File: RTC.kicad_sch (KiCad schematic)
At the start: 10 parts, among them J17 Molex 470531000, J2 Molex 470531000, J3 Molex 470531000, J6 Molex 470531000, U2 EMC2305-1-AP-TR

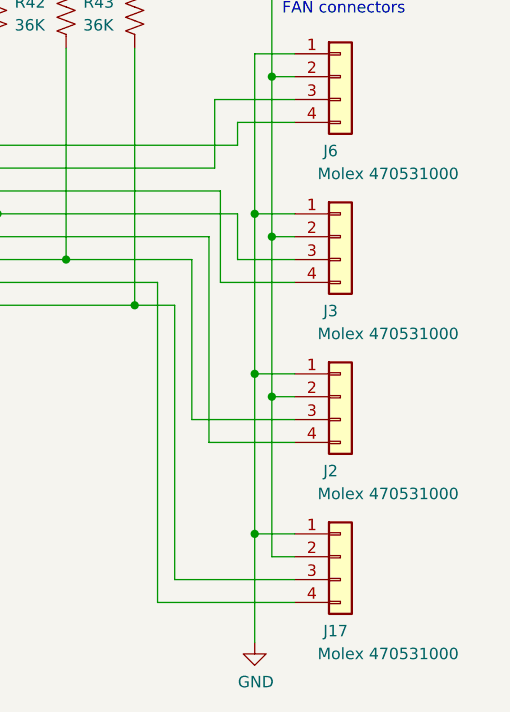
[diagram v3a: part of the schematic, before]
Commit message: added the right board outline. rotated the CM4. switched to single-shroud RA fan connectors
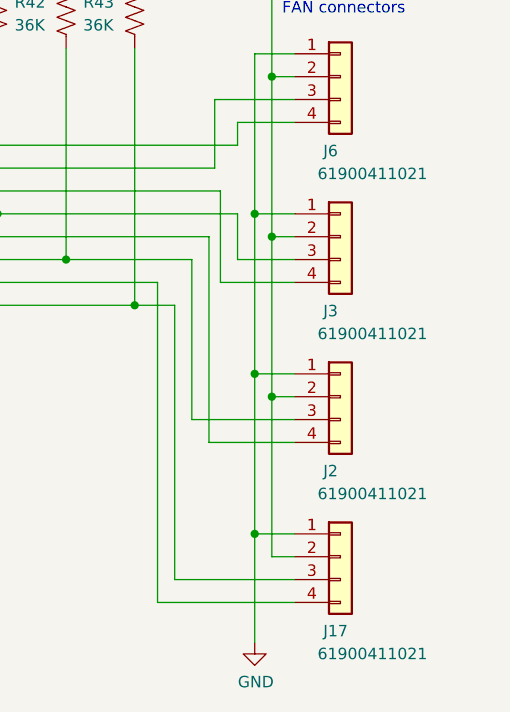
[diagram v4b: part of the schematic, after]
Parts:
- J17, J2, J3: value Molex 470531000 -> 61900411021; footprint Connector:FanPinHeader_1x04_P2.54mm_Vertical -> bitcart:CONN_61900411021_WRE; DK WM4330-ND -> 732-2701-ND; Field4 Farnell -> (none); Field5 2313705 -> (none); Field6 470531000 -> (none); Field7 Molex -> (none); PARTNO 470531000 -> 61900411021
- J6: value Molex 470531000 -> 61900411021; footprint Connector:FanPinHeader_1x04_P2.54mm_Vertical -> bitcart:CONN_61900411021_WRE; DK WM4330-ND -> 732-2701-ND; Field6 470531000 -> (none); PARTNO 470531000 -> 61900411021
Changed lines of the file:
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@@
       (effects (font (size 1.27 1.27)) (justify left))
     )
-    (property "Value" "Molex 470531000" (at 194.31 121.285 0)
-      (effects (font (size 1.27 1.27)) (justify left))
-    )
-    (property "Footprint" "Connector:FanPinHeader_1x04_P2.54mm_Vertical" (at 196.85 110.49 0)
+    (property "Value" "61900411021" (at 194.31 121.285 0)
+      (effects (font (size 1.27 1.27)) (justify left))
+    )
+    (property "Footprint" "bitcart:CONN_61900411021_WRE" (at 196.85 110.49 0)
       (effects (font (size 1.27 1.27)) hide)
     )
@@
       (effects (font (size 1.27 1.27)) hide)
     )
-    (property "Field4" "Farnell" (at 196.85 110.49 0)
-      (effects (font (size 1.27 1.27)) hide)
-    )
-    (property "Field5" "	2313705" (at 196.85 110.49 0)
-      (effects (font (size 1.27 1.27)) hide)
-    )
-    (property "Field6" "470531000" (at 196.85 110.49 0)
-      (effects (font (size 1.27 1.27)) hide)
-    )
-    (property "Field7" "Molex" (at 196.85 110.49 0)
-      (effects (font (size 1.27 1.27)) hide)
-    )
-    (property "Part Description" "" (at 196.85 110.49 0)
-      (effects (font (size 1.27 1.27)) hide)
-    )
-    (property "DK" "WM4330-ND" (at 196.85 110.49 0)
-      (effects (font (size 1.27 1.27)) hide)
-    )
-    (property "PARTNO" "470531000" (at 196.85 110.49 0)
+    (property "DK" "732-2701-ND" (at 196.85 110.49 0)
+      (effects (font (size 1.27 1.27)) hide)
+    )
+    (property "PARTNO" "61900411021" (at 196.85 110.49 0)
       (effects (font (size 1.27 1.27)) hide)
     )
@@
       (effects (font (size 1.27 1.27)) (justify left))
     )
-    (property "Value" "Molex 470531000" (at 194.31 67.945 0)
-      (effects (font (size 1.27 1.27)) (justify left))
-    )
-    (property "Footprint" "Connector:FanPinHeader_1x04_P2.54mm_Vertical" (at 196.85 57.15 0)
+    (property "Value" "61900411021" (at 194.31 67.945 0)
+      (effects (font (size 1.27 1.27)) (justify left))
+    )
+    (property "Footprint" "bitcart:CONN_61900411021_WRE" (at 196.85 57.15 0)
       (effects (font (size 1.27 1.27)) hide)
     )
@@
       (effects (font (size 1.27 1.27)) hide)
     )
-    (property "DK" "WM4330-ND" (at 196.85 57.15 0)
-      (effects (font (size 1.27 1.27)) hide)
-    )
-    (property "Field6" "470531000" (at 196.85 57.15 0)
-      (effects (font (size 1.27 1.27)) hide)
-    )
-    (property "PARTNO" "470531000" (at 196.85 57.15 0)
+    (property "DK" "732-2701-ND" (at 196.85 57.15 0)
+      (effects (font (size 1.27 1.27)) hide)
+    )
+    (property "PARTNO" "61900411021" (at 196.85 57.15 0)
       (effects (font (size 1.27 1.27)) hide)
     )
@@
       (effects (font (size 1.27 1.27)) (justify left))
     )
-    (property "Value" "Molex 470531000" (at 194.31 103.505 0)
-      (effects (font (size 1.27 1.27)) (justify left))
-    )
-    (property "Footprint" "Connector:FanPinHeader_1x04_P2.54mm_Vertical" (at 196.85 92.71 0)
+    (property "Value" "61900411021" (at 194.31 103.505 0)
+      (effects (font (size 1.27 1.27)) (justify left))
+    )
+    (property "Footprint" "bitcart:CONN_61900411021_WRE" (at 196.85 92.71 0)
       (effects (font (size 1.27 1.27)) hide)
     )
@@
       (effects (font (size 1.27 1.27)) hide)
     )
-    (property "Field4" "Farnell" (at 196.85 92.71 0)
-      (effects (font (size 1.27 1.27)) hide)
-    )
-    (property "Field5" "	2313705" (at 196.85 92.71 0)
-      (effects (font (size 1.27 1.27)) hide)
-    )
-    (property "Field6" "470531000" (at 196.85 92.71 0)
-      (effects (font (size 1.27 1.27)) hide)
-    )
-    (property "Field7" "Molex" (at 196.85 92.71 0)
-      (effects (font (size 1.27 1.27)) hide)
-    )
-    (property "Part Description" "" (at 196.85 92.71 0)
-      (effects (font (size 1.27 1.27)) hide)
-    )
-    (property "DK" "WM4330-ND" (at 196.85 92.71 0)
-      (effects (font (size 1.27 1.27)) hide)
-    )
-    (property "PARTNO" "470531000" (at 196.85 92.71 0)
+    (property "DK" "732-2701-ND" (at 196.85 92.71 0)
+      (effects (font (size 1.27 1.27)) hide)
+    )
+    (property "PARTNO" "61900411021" (at 196.85 92.71 0)
       (effects (font (size 1.27 1.27)) hide)
     )
@@
       (effects (font (size 1.27 1.27)) (justify left))
     )
-    (property "Value" "Molex 470531000" (at 194.31 85.725 0)
-      (effects (font (size 1.27 1.27)) (justify left))
-    )
-    (property "Footprint" "Connector:FanPinHeader_1x04_P2.54mm_Vertical" (at 196.85 74.93 0)
+    (property "Value" "61900411021" (at 194.31 85.725 0)
+      (effects (font (size 1.27 1.27)) (justify left))
+    )
+    (property "Footprint" "bitcart:CONN_61900411021_WRE" (at 196.85 74.93 0)
       (effects (font (size 1.27 1.27)) hide)
     )
@@
       (effects (font (size 1.27 1.27)) hide)
     )
-    (property "Field4" "Farnell" (at 196.85 74.93 0)
-      (effects (font (size 1.27 1.27)) hide)
-    )
-    (property "Field5" "	2313705" (at 196.85 74.93 0)
-      (effects (font (size 1.27 1.27)) hide)
-    )
-    (property "Field6" "470531000" (at 196.85 74.93 0)
-      (effects (font (size 1.27 1.27)) hide)
-    )
-    (property "Field7" "Molex" (at 196.85 74.93 0)
-      (effects (font (size 1.27 1.27)) hide)
-    )
-    (property "Part Description" "" (at 196.85 74.93 0)
-      (effects (font (size 1.27 1.27)) hide)
-    )
-    (property "DK" "WM4330-ND" (at 196.85 74.93 0)
-      (effects (font (size 1.27 1.27)) hide)
-    )
-    (property "PARTNO" "470531000" (at 196.85 74.93 0)
-      (effects (font (size 1.27 1.27)) hide)
-    )
+    (property "DK" "732-2701-ND" (at 196.85 74.93 0)
+      (effects (font (size 1.27 1.27)) hide)
+    )
+    (property "PARTNO" "61900411021" (at 196.85 74.93 0)
+      (effects (font (size 1.27 1.27)) hide)
+    )

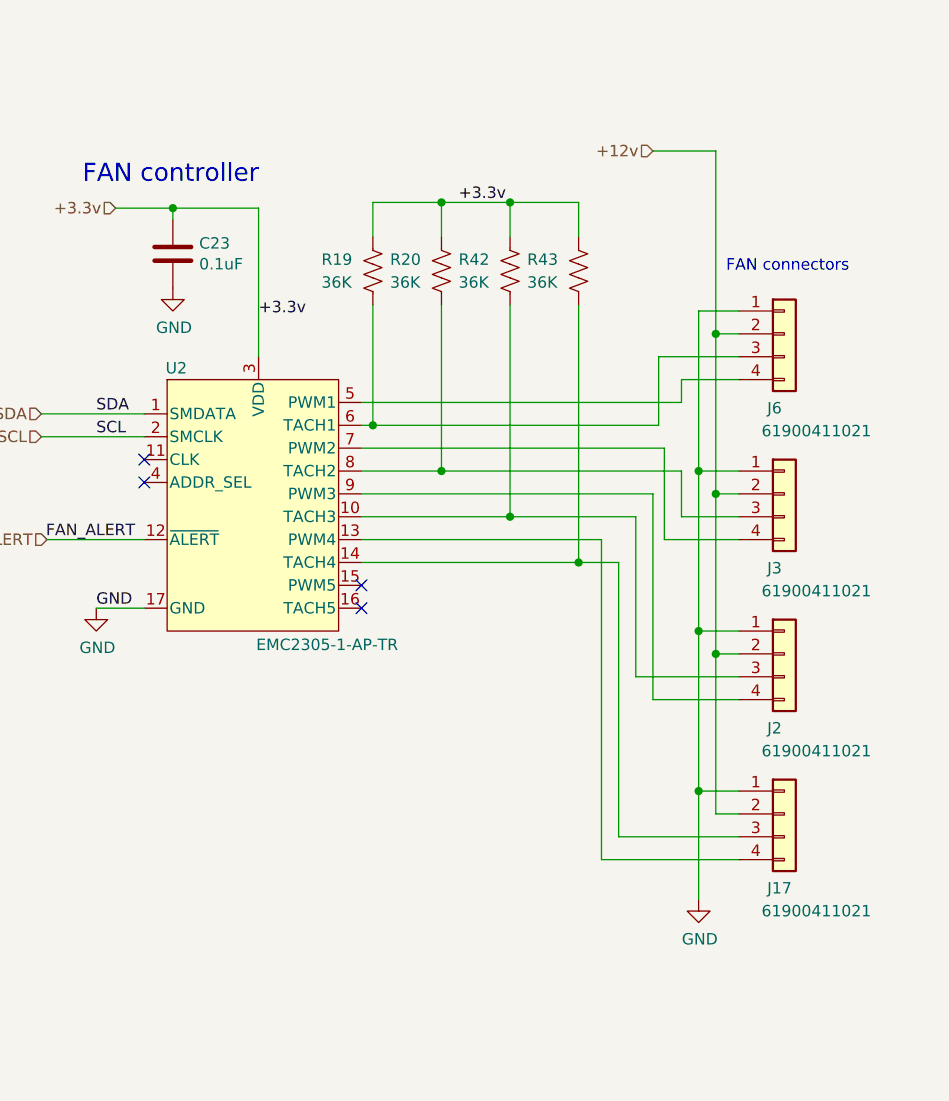
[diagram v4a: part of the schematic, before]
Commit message: resolved some schematic-board errors. switched to tap-on-top ethernet.
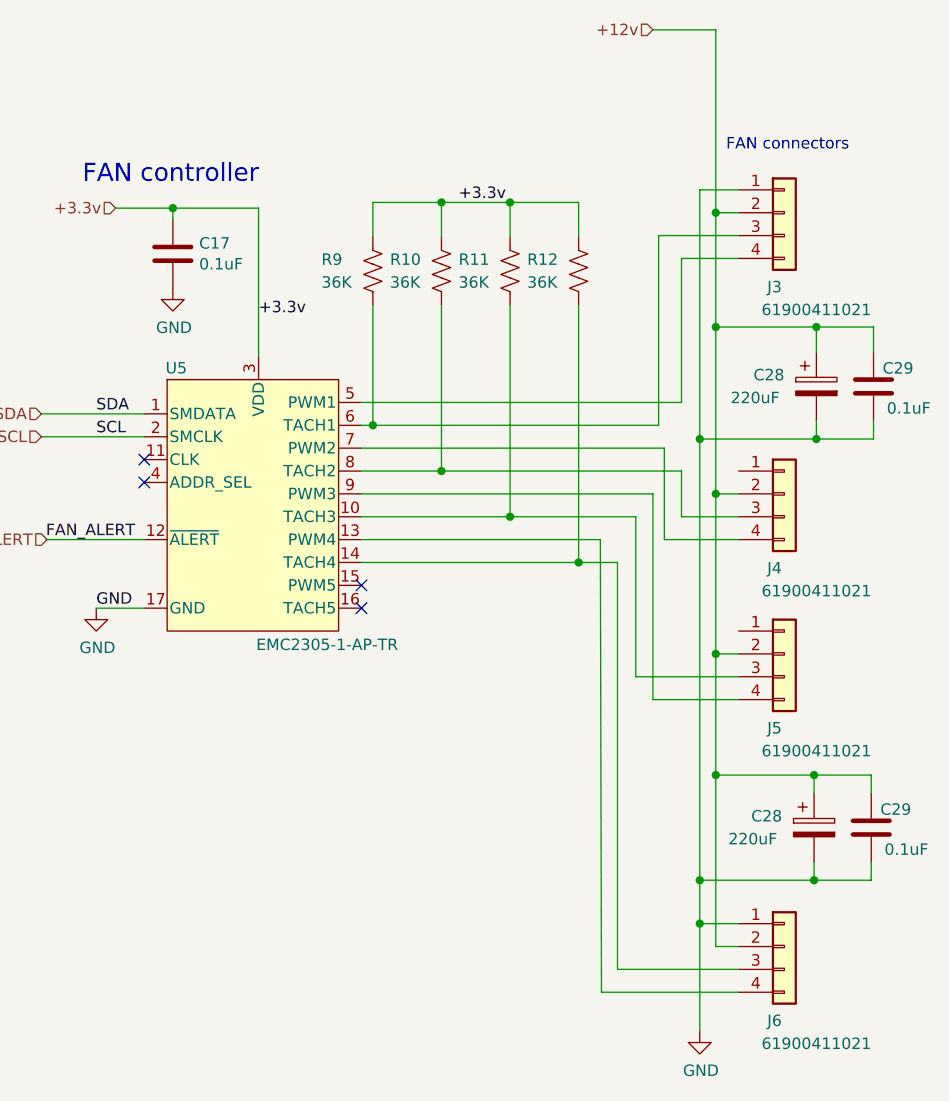
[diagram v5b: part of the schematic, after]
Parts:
- added C28 (x2): 220uF, Capacitor_SMD:CP_Elec_6.3x7.7, symbol Device:C_Polarized
- added C29 (x2): 0.1uF, Capacitor_SMD:C_0402_1005Metric, symbol Device:C
- renumbered C23 to C17, J6 to J3, J3 to J4, J2 to J5, J17 to J6, R20 to R10, R42 to R11, R43 to R12, R19 to R9, U2 to U5
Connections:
- net +12v: now also C28.1, C28.1, C29.1, C29.1
- net GND: now also C28.2, C28.2, C29.2, C29.2; no longer J4.1 (Pin_1), J5.1 (Pin_1)
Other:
- moved on the sheet: J3, J6

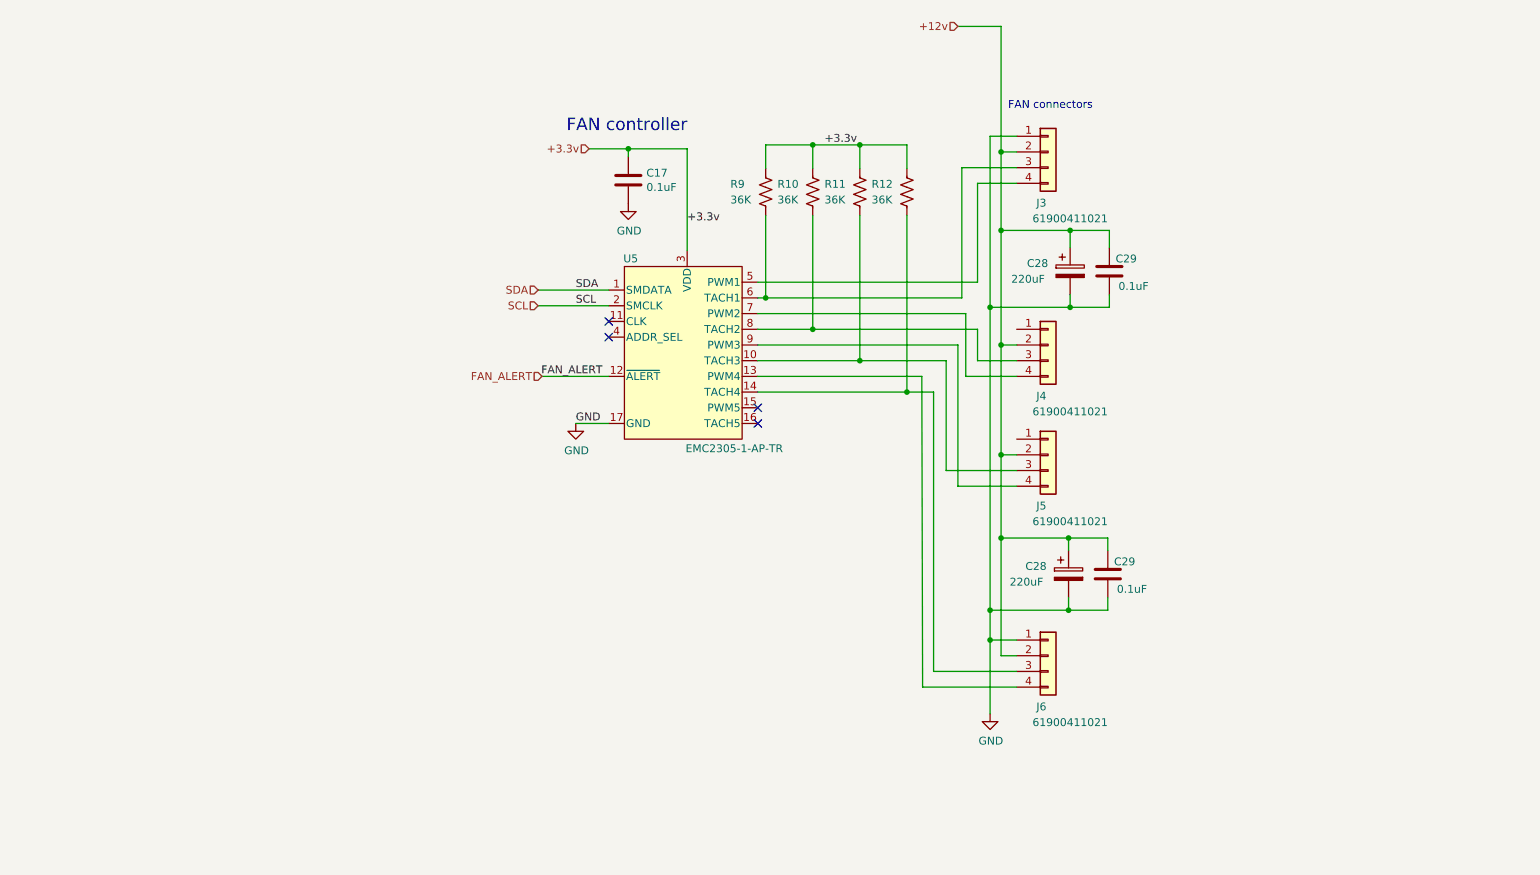
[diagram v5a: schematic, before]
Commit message: pulled in bitcrane fan and data connectors and edge cuts. most placement done. started routing
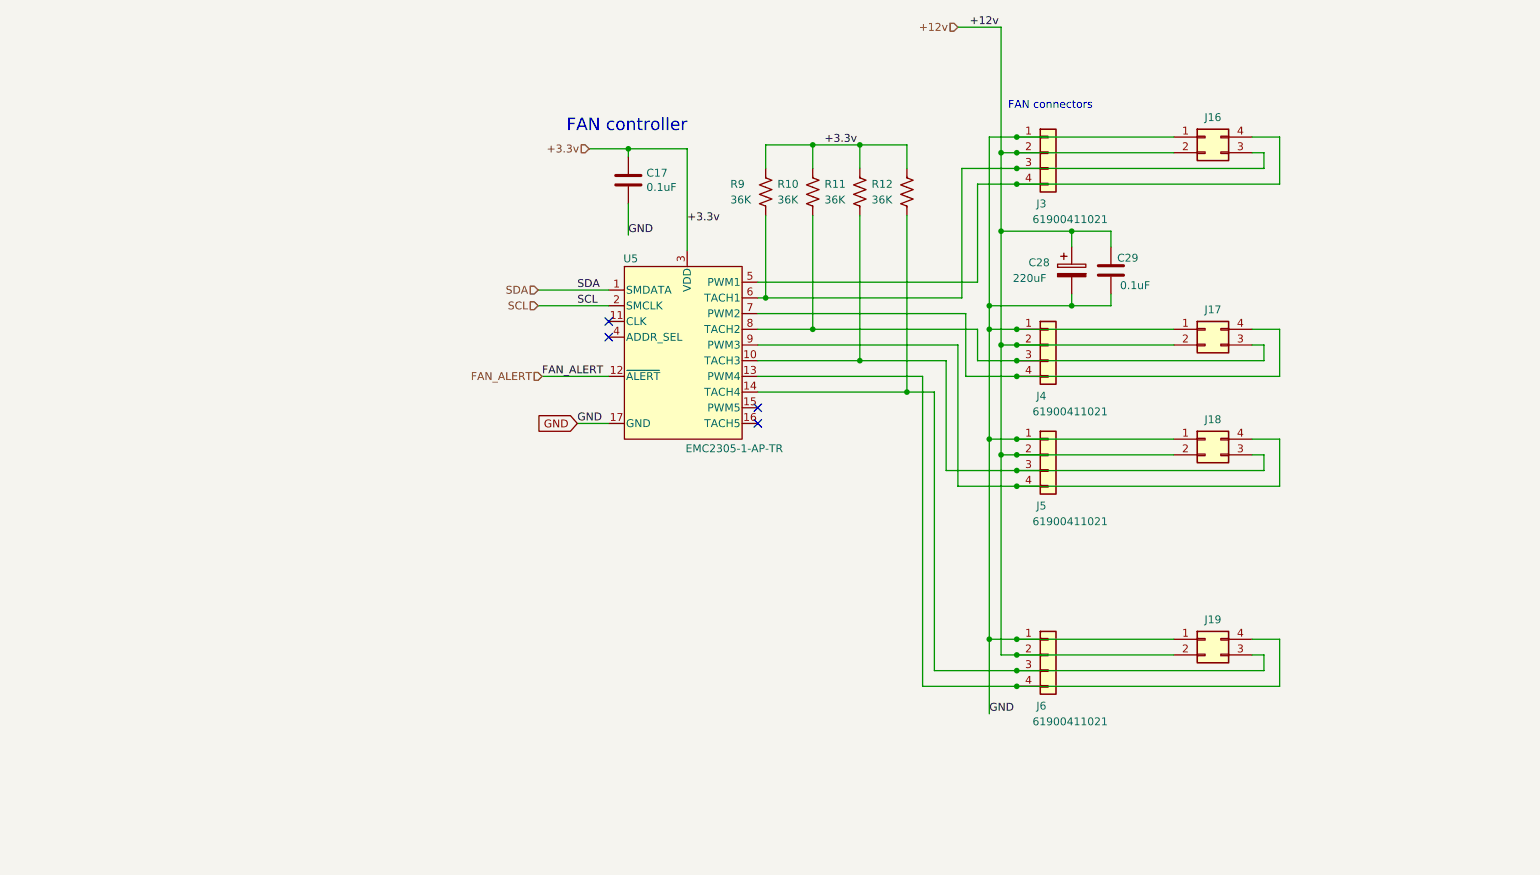
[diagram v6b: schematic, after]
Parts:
- removed C28: 220uF, Capacitor_SMD:CP_Elec_6.3x7.7, symbol Device:C_Polarized
- removed C29: 0.1uF, Capacitor_SMD:C_0402_1005Metric, symbol Device:C
- added J16, J17, J18, J19: 0353180420, bitcrane:MOLEX_353180420, symbol Connector_Generic:Conn_02x02_Counter_Clockwise
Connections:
- net +12v: now also J16.2 (Pin_2), J17.2 (Pin_2), J18.2 (Pin_2), J19.2 (Pin_2)
- net GND: now also J4.1 (Pin_1), J5.1 (Pin_1), J16.1 (Pin_1), J17.1 (Pin_1), J18.1 (Pin_1), J19.1 (Pin_1)
- net at J6.3 (Pin_3), R12.2, U5.14 (TACH4): now also J19.3 (Pin_3)
- net at J6.4 (Pin_4), U5.13 (PWM4): now also J19.4 (Pin_4)
- net at J5.3 (Pin_3), R11.2, U5.10 (TACH3): now also J18.3 (Pin_3)
- net at J3.4 (Pin_4), U5.5 (PWM1): now also J16.4 (Pin_4)
- net at J3.3 (Pin_3), R9.2, U5.6 (TACH1): now also J16.3 (Pin_3)
- net at J4.4 (Pin_4), U5.7 (PWM2): now also J17.4 (Pin_4)
- net at J4.3 (Pin_3), R10.2, U5.8 (TACH2): now also J17.3 (Pin_3)
- net at J5.4 (Pin_4), U5.9 (PWM3): now also J18.4 (Pin_4)

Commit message: lots of routing. lots more to do
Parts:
- added R19, R20, R21, R22: 10k, Resistor_SMD:R_0402_1005Metric, symbol Device:R_US
- R10, R11, R12, R9: value 36K -> 36k
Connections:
- net at J19.4 (Pin_4), J6.4 (Pin_4), U5.13 (PWM4): now also R21.2
- net at J16.4 (Pin_4), J3.4 (Pin_4), U5.5 (PWM1): now also R19.2
- net at J17.4 (Pin_4), J4.4 (Pin_4), U5.7 (PWM2): now also R20.2
- net at J18.4 (Pin_4), J5.4 (Pin_4), U5.9 (PWM3): now also R22.2
- net +12v renamed 12V
- net +3.3v renamed 3V3
- new net 5V: R19.1, R20.1, R21.1, R22.1
